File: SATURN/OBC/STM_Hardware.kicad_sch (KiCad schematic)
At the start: 10 parts, among them J1 SWD Pins, J2 USB_OTG, U1 USBLC6-4SC6, U2 RV-3028-C7 32.768KHZ 1PPM-TA-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

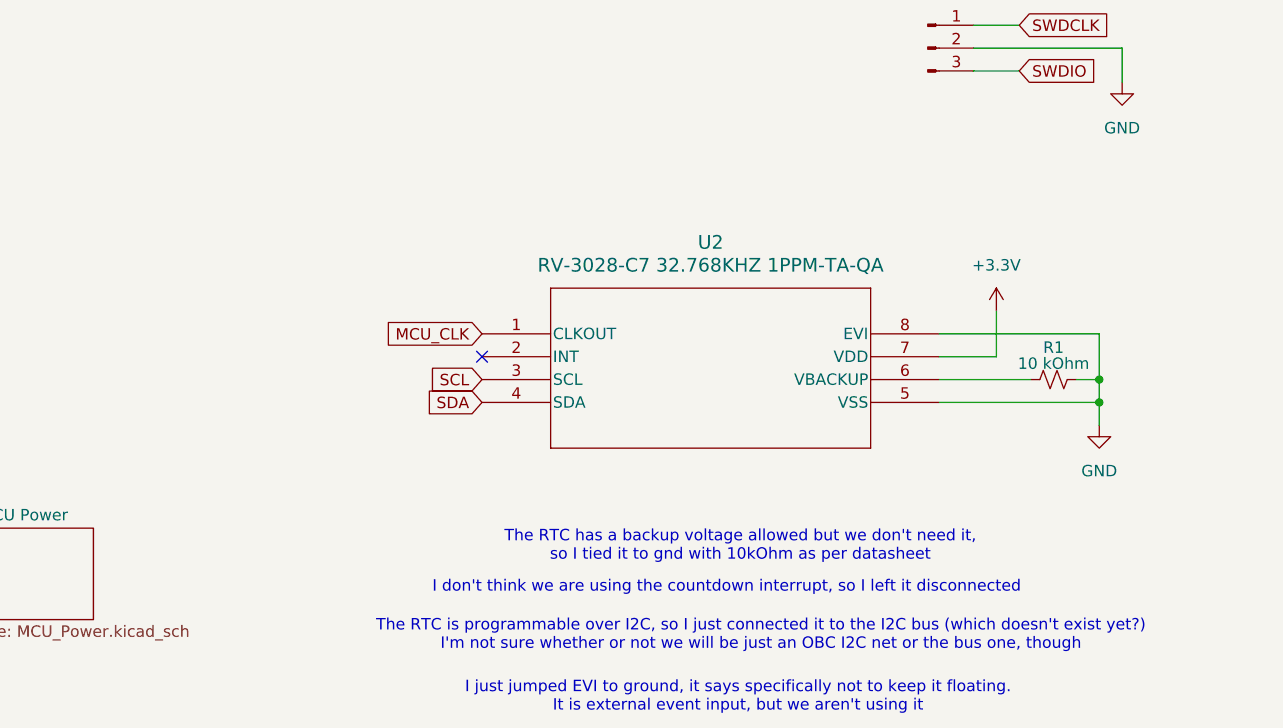
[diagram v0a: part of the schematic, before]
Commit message: Added backup battery to RTC
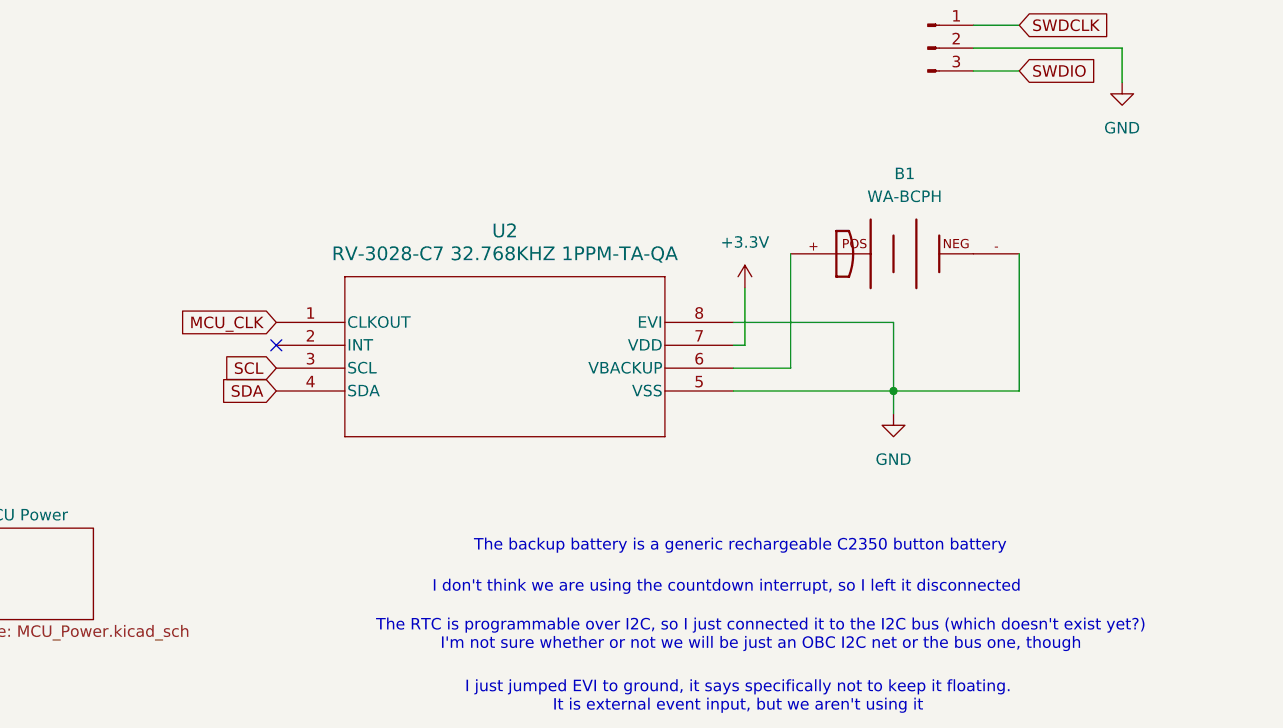
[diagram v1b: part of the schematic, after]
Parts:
- removed R1: 10 kOhm, symbol Device:R_Small_US
- added B1: WA-BCPH, WA-BCPH:WA-BCPH_79578211, symbol OBC-Components-lin:WA-BCPH
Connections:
- net GND: now also B1.-
- net at U2.6 (VBACKUP): now also B1.+
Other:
- note added: "The backup battery is a generic rechargeable C2350 button battery"
- note removed: "The RTC has a backup voltage allowed but we don't need it, so I tied it to gnd with 10kOhm as per datasheet"
- moved on the sheet: U2

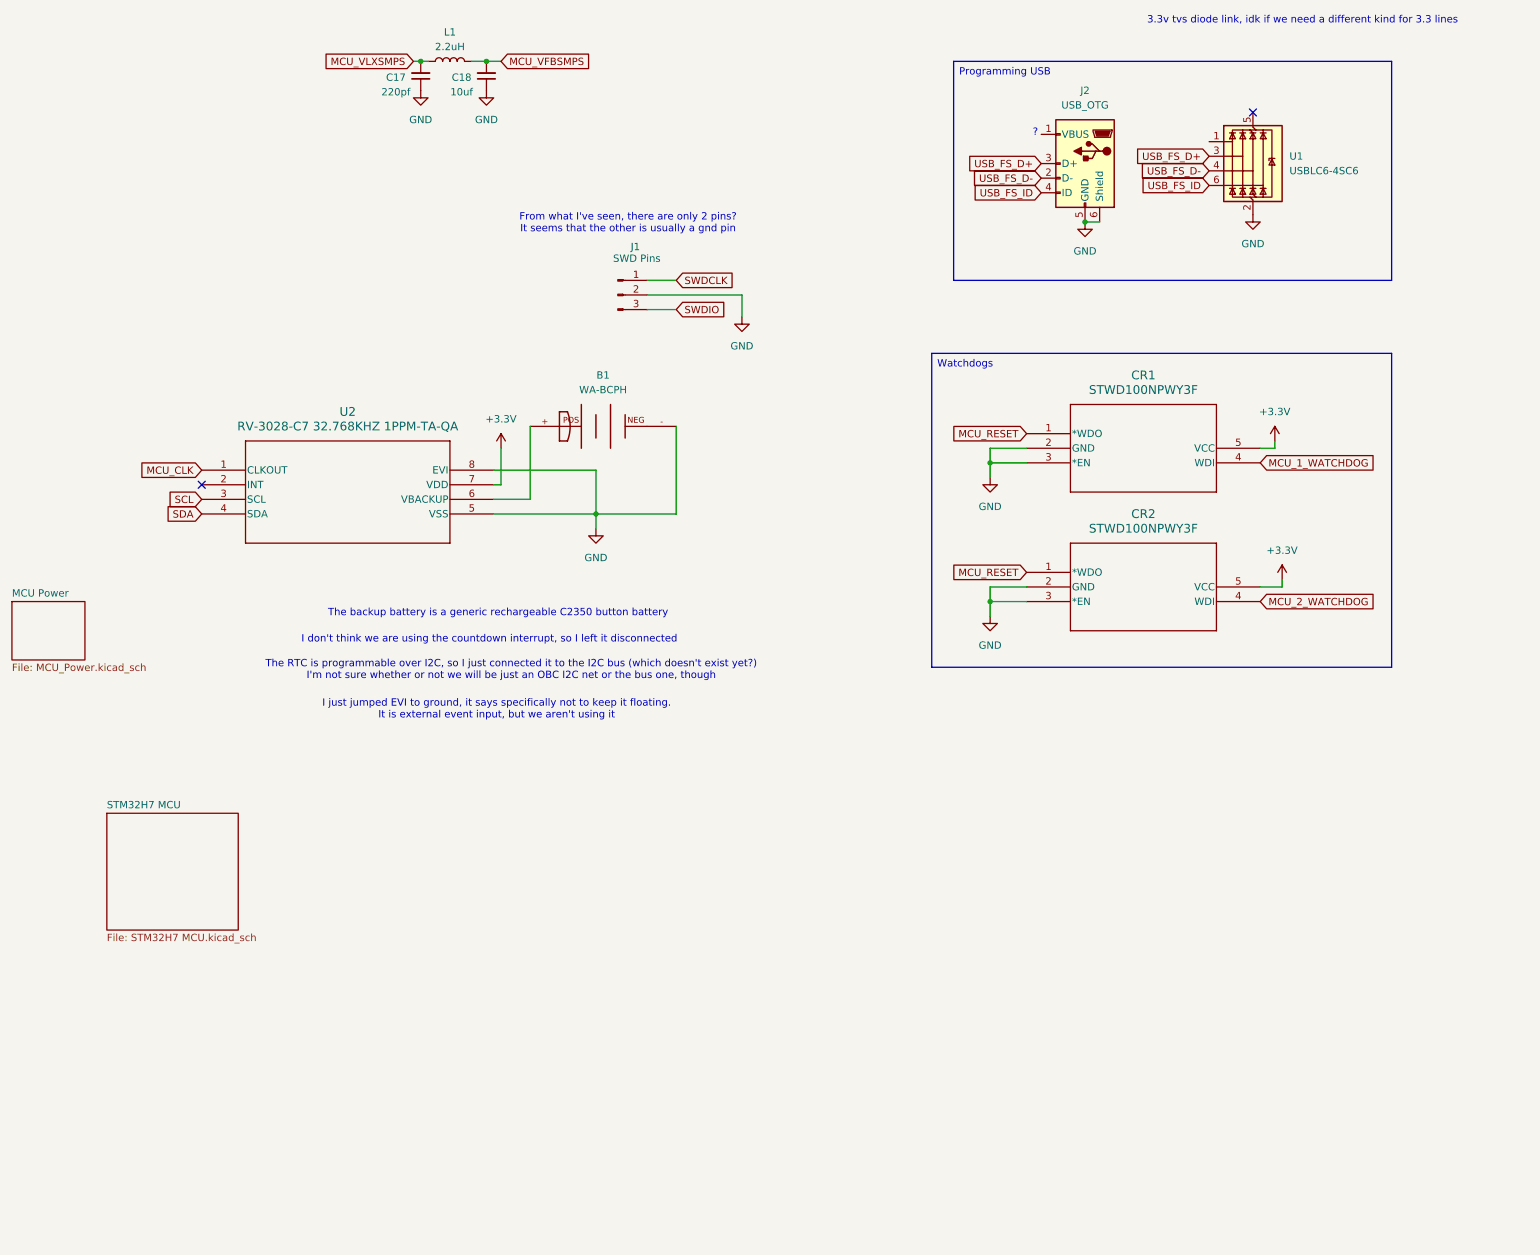
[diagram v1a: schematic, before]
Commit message: Added USB switcher and updated to MCUs
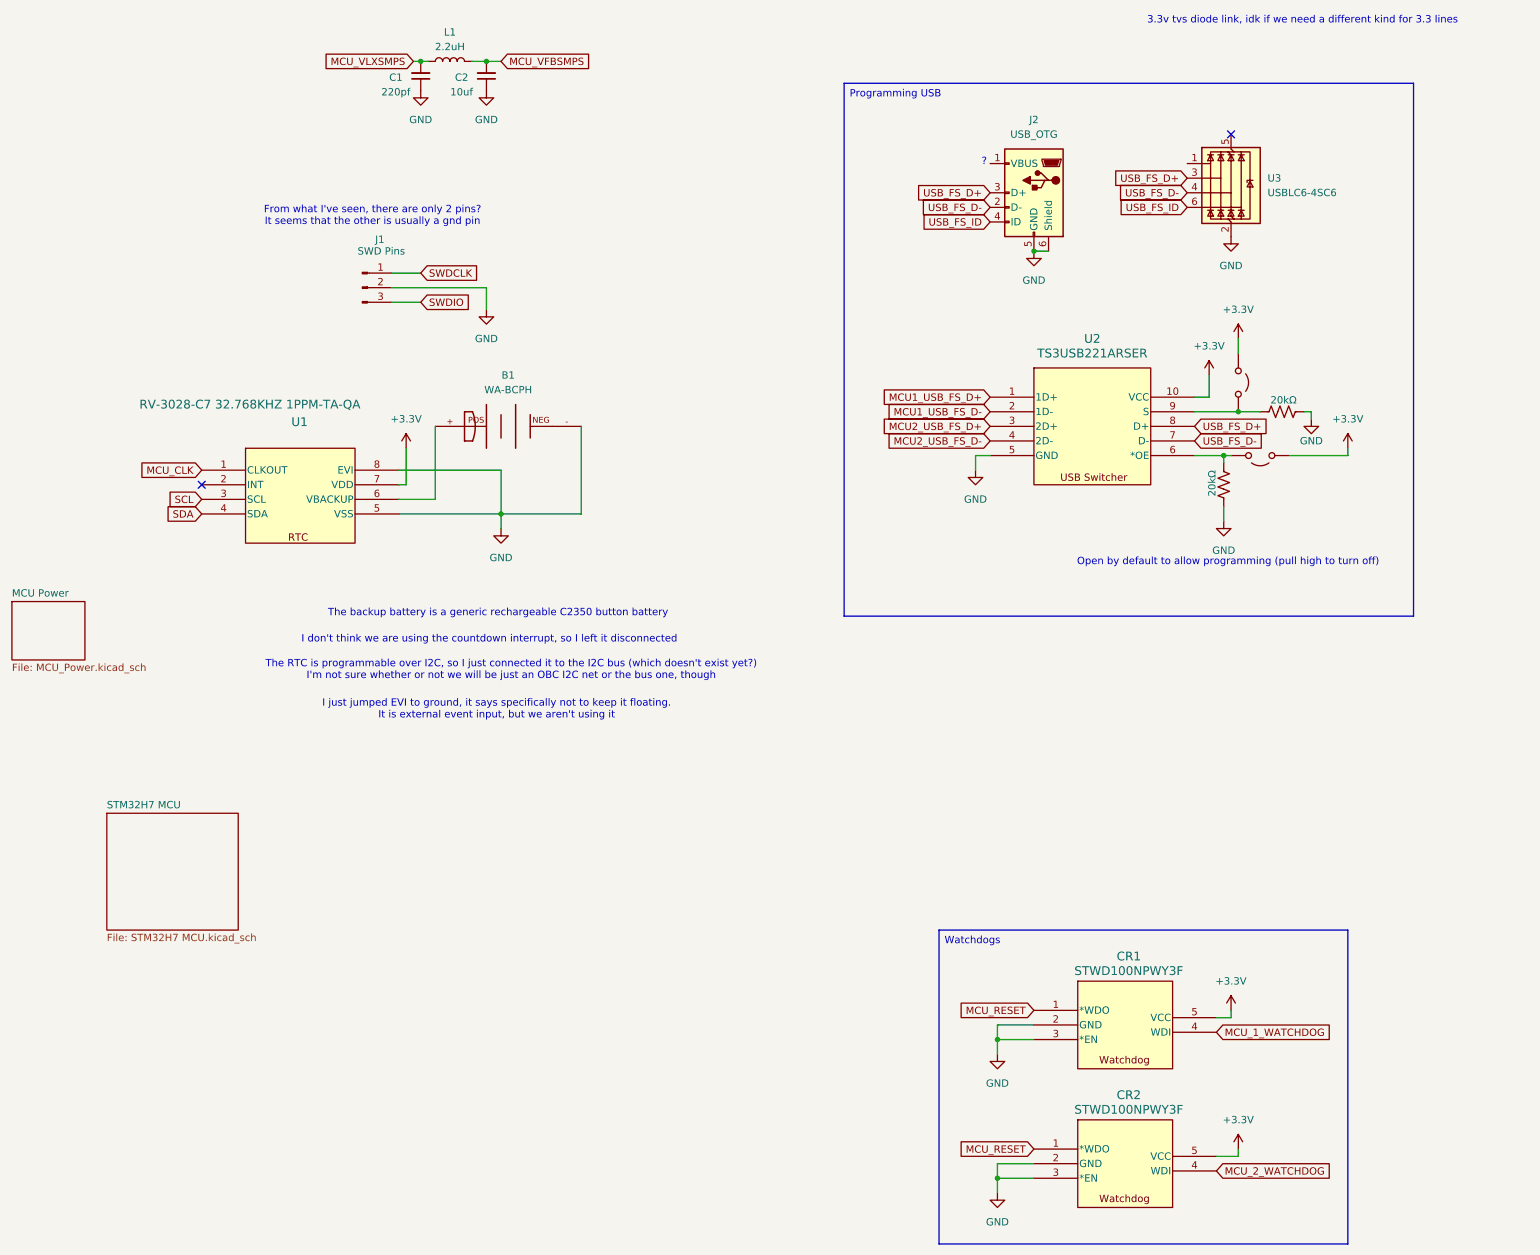
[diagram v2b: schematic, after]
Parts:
- added JP1, JP2: Jumper_2_Open, symbol Jumper:Jumper_2_Open
- added R1, R2: 20kΩ, symbol Device:R_US
- added U2: TS3USB221ARSER, RSE10, symbol OBC-Components-lin:TS3USB221ARSER
- J1: footprint (none) -> Connector_PinHeader_1.27mm:PinHeader_1x03_P1.27mm_Vertical
- renumbered C17 to C1, C18 to C2, U2 to U1, U1 to U3
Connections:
- net +3.3V: now also JP1.1 (A), JP2.1 (A), U2.10 (VCC)
- net GND: now also R1.2, R2.1, U2.5 (GND)
- net USB_FS_D+: now also U2.8 (D+)
- net USB_FS_D-: now also U2.7 (D-)
- new net: JP1.2 (B), R2.2, U2.9 (S)
- new net: JP2.2 (B), R1.1, U2.6 (*OE)
- new net MCU1_USB_FS_D+: U2.1 (1D+)
- new net MCU1_USB_FS_D-: U2.2 (1D-)
- new net MCU2_USB_FS_D+: U2.3 (2D+)
- new net MCU2_USB_FS_D-: U2.4 (2D-)
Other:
- note added: "Open by default to allow programming (pull high to turn off)"
- moved on the sheet: B1, J1, J2, U3
